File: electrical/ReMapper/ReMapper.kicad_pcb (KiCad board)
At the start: 4 copper layers, 35 x 65 mm, 43 parts, among them J1 ESP_UART0, J2 I2C Display, J3 USB_IN, J4 USB_OUT, J5 Button GND Pad, J9 Button Socket, U1 SPX1117M3-L-3-3/TR, U2 W25Q128JVE, U3 ESP32-S3-WROOM-1-N8R8, U4 RP2040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

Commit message: started working on v5
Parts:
- removed G***: LOGO, LOGO
- removed J1: ESP_UART0, Connector_PinHeader_1.27mm:PinHeader_1x04_P1.27mm_Vertical_SMD_Pin1Right
- removed J9: Button Socket, Connector_PinHeader_1.27mm:PinHeader_1x04_P1.27mm_Vertical_SMD_Pin1Left
- removed JP1: RP2040 Prog, Jumper:SolderJumper-2_P1.3mm_Open_RoundedPad1.0x1.5mm
- added S3: ESP_B1, generated_lscs:SW-SMD_4P-L4.5-W4.5-P3.00-LS6.8, F.Cu at (169.1, 115.0)
- added S4: ESP_B2, generated_lscs:SW-SMD_4P-L4.5-W4.5-P3.00-LS6.8, F.Cu at (185.1, 115.0)
- added S5: ESP_B3, generated_lscs:SW-SMD_4P-L4.5-W4.5-P3.00-LS6.8, F.Cu at (200.8, 115.0)
- added S6: ESP_B4_prog, generated_lscs:SW-SMD_4P-L4.5-W4.5-P3.00-LS6.8, F.Cu at (150.8, 115.0)
- C10, C13, C14, U4, U5: moved to B.Cu
- J2: footprint Connector_PinHeader_1.27mm:PinHeader_1x04_P1.27mm_Vertical -> Connector_PinHeader_2.54mm:PinHeader_1x04_P2.54mm_Vertical; moved to F.Cu
- J5: value Button GND Pad -> Conn_01x06_Pin; footprint TestPoint:TestPoint_Pad_D2.0mm -> cedarhacks:pogo_pin_2.54mm
- moved J3 69.7 mm to (142.6, 90.2), turned to -90 degrees
- moved LED5 69.3 mm to (144.0, 106.0), turned to 0 degrees
- moved R8 66.8 mm to (147.6, 106.0), turned to 180 degrees
- moved LED3 65.6 mm to (144.0, 102.6), turned to 0 degrees
- moved R6 63.9 mm to (147.6, 102.6), turned to 180 degrees
- moved R1 56.9 mm to (148.0, 115.4), turned to 180 degrees
- moved S1 55.7 mm to (156.8, 116.4)
- moved C2 55.5 mm to (151.6, 115.4), turned to 180 degrees
- moved C11 54.8 mm to (204.7, 108.6), turned to 90 degrees
- moved Y1 52.4 mm to (200.7, 108.4), turned to 180 degrees
- moved D1 51.9 mm to (154.1, 105.5), turned to 180 degrees
- moved C12 51.5 mm to (197.0, 109.4), turned to -90 degrees
- moved C8 51.4 mm to (165.1, 117.8), turned to -90 degrees
- moved D2 51.0 mm to (154.2, 103.9), turned to 0 degrees
- moved R2 50.4 mm to (196.2, 106.4), turned to 180 degrees
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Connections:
- J5 pad 1: GND -> /3.3V
- R5 pad 1: Net-(JP1-B) -> /RP2040_PROG
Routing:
- net GND: track 71.6 -> 0.00 mm, vias 26 -> 0
- net /USB_VIN: track 68.6 -> 0.00 mm, vias 3 -> 0
- net /USB_OUT_D-: track 45.8 -> 0.00 mm, vias 2 -> 0
- net /USB_OUT_D+: track 45.8 -> 0.00 mm, vias 1 -> 0
- net /3.3V: track 40.1 -> 0.00 mm, vias 17 -> 0
- net /QSPI_IO0_esp: track 38.3 -> 0.00 mm, vias 2 -> 0
- net /SPI2_MISO: track 37.8 -> 0.00 mm, vias 1 -> 0
- net /QSPI_CLK_esp: track 36.7 -> 0.00 mm, vias 2 -> 0
- net /SPI2_CLK: track 36.4 -> 0.00 mm, vias 1 -> 0
- net /QSPI_IO3_esp: track 35.4 -> 0.00 mm
- net /QSPI_IO2_esp: track 33.8 -> 0.00 mm, vias 2 -> 0
- net /SPI2_CS: track 32.2 -> 0.00 mm, vias 1 -> 0
- net /SPI2_MOSI: track 31.7 -> 0.00 mm, vias 1 -> 0
- net /QSPI_IO1_esp: track 31.1 -> 0.00 mm, vias 2 -> 0
- net /ESP_BUTTON_3: track 24.2 -> 0.00 mm, vias 1 -> 0
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- removed copper zone on In2.Cu, net /3.3V
- removed copper zone on In1.Cu, net GND
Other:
- board size 35 x 65 mm -> 75 x 55 mm
- board text removed: "3.3V"
- board text removed: "33V"
- board text removed: "33V LED"
- board text removed: "B1"
- board text removed: "B2"
- board text removed: "B3"
- board text removed: "CLK"
- board text removed: "D+"
- board text removed: "D-"
- board text removed: "DATA"
- board text removed: "ESP ENB"
- board text removed: "ESP LED"
- board text removed: "ESP UART"
- board text removed: "ESP prog"
- board text removed: "GND"
- board text removed: "PROG"
- board text removed: "RX"
- board text removed: "ReMapper Rev4 CedarHacks.com"
- board text removed: "TX"
- board text removed: "VIN"

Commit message: perhaps good layout
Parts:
- added ?: , , F.Cu at (189.8, 102.7)
- added ?: , , F.Cu at (189.8, 79.2)
- added ?: , , F.Cu at (166.8, 79.2)
- added ?: , , F.Cu at (166.8, 102.7)
- moved C13 4.56 mm to (189.1, 84.1)
- moved D3 4.04 mm to (160.4, 103.6)
- moved D4 4.04 mm to (160.4, 101.8)
- moved C14 3.06 mm to (189.1, 85.9)
- moved J3 0.19 mm to (142.6, 90.1)
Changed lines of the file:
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@@
 		)
 	)
+	(footprint ""
+		(layer "F.Cu")
+		(at 189.8176 102.681599)
+		(property "Reference" ""
+			(at 0 0 0)
+			(layer "F.SilkS")
+			(effects
+				(font
+					(size 1.27 1.27)
+					(thickness 0.15)
+				)
+			)
+		)
+		(property "Value" ""
+			(at 0 0 0)
+			(layer "F.Fab")
+			(effects
+				(font
+					(size 1.27 1.27)
+					(thickness 0.15)
+				)
+			)
+		)
+		(property "Datasheet" ""
+			(at 0 0 0)
+			(layer "F.Fab")
+			(hide yes)
+			(effects
+				(font
+					(size 1.27 1.27)
+					(thickness 0.15)
+				)
+			)
+		)
+		(property "Description" ""
+			(at 0 0 0)
+			(layer "F.Fab")
+			(hide yes)
+			(effects
+				(font
+					(size 1.27 1.27)
+					(thickness 0.15)
+				)
+			)
+		)
+		(pad "" np_thru_hole circle
+			(at 0 0)
+			(size 2.2 2.2)
+			(drill 2.2)
+			(layers "*.Cu" "*.Mask")
+		)
+		(embedded_fonts no)
+	)
 	(footprint "Resistor_SMD:R_0603_1608Metric"
 		(layer "F.Cu")
@@
 		)
 	)
+	(footprint ""
+		(layer "F.Cu")
+		(at 189.8176 79.181599)
+		(property "Reference" ""
+			(at 0 0 0)
+			(layer "F.SilkS")
+			(effects
+				(font
+					(size 1.27 1.27)
+					(thickness 0.15)
+				)
+			)
+		)
+		(property "Value" ""
+			(at 0 0 0)
+			(layer "F.Fab")
+			(effects
+				(font
+					(size 1.27 1.27)
+					(thickness 0.15)
+				)
+			)
+		)
+		(property "Datasheet" ""
+			(at 0 0 0)
+			(layer "F.Fab")
+			(hide yes)
+			(effects
+				(font
+					(size 1.27 1.27)
+					(thickness 0.15)
+				)
+			)
+		)
+		(property "Description" ""
+			(at 0 0 0)
+			(layer "F.Fab")
+			(hide yes)
+			(effects
+				(font
+					(size 1.27 1.27)
+					(thickness 0.15)
+				)
+			)
+		)
+		(pad "" np_thru_hole circle
+			(at 0 0)
+			(size 2.2 2.2)
+			(drill 2.2)
+			(layers "*.Cu" "*.Mask")
+		)
+		(embedded_fonts no)
+	)
 	(footprint "generated_lscs:SW-SMD_4P-L4.5-W4.5-P3.00-LS6.8"
 		(layer "F.Cu")
@@
 			(at -3.068401 3.2424 180)
 			(layer "F.Fab")
+			(hide yes)
 			(effects
 				(font
@@
 			(at 0 1.43 90)
 			(layer "F.Fab")
+			(hide yes)
 			(effects
 				(font
@@
 	(footprint "footprints:USBA_Female"
 		(layer "F.Cu")
-		(at 142.565 90.25 -90)
+		(at 142.565 90.059 -90)
 		(property "Reference" "J3"
 			(at 9.191 -6.025 90)
@@
 		(embedded_fonts no)
 	)
+	(footprint ""
+		(layer "F.Cu")
+		(at 166.8176 79.181599)
+		(property "Reference" ""
+			(at 0 0 0)
+			(layer "F.SilkS")
+			(effects
+				(font
+					(size 1.27 1.27)
+					(thickness 0.15)
+				)
+			)
+		)
+		(property "Value" ""
+			(at 0 0 0)
+			(layer "F.Fab")
+			(effects
+				(font
+					(size 1.27 1.27)
+					(thickness 0.15)
+				)
+			)
+		)
+		(property "Datasheet" ""
+			(at 0 0 0)
+			(layer "F.Fab")
+			(hide yes)
+			(effects
+				(font
+					(size 1.27 1.27)
+					(thickness 0.15)
+				)
+			)
+		)
+		(property "Description" ""
+			(at 0 0 0)
+			(layer "F.Fab")
+			(hide yes)
+			(effects
+				(font
+					(size 1.27 1.27)
+					(thickness 0.15)
+				)
+			)
+		)
+		(pad "" np_thru_hole circle
+			(at 0 0)
+			(size 2.2 2.2)
+			(drill 2.2)
+			(layers "*.Cu" "*.Mask")
+		)
+		(embedded_fonts no)
+	)
 	(footprint "Capacitor_SMD:C_0603_1608Metric"
 		(layer "F.Cu")
@@
 		)
 	)
+	(footprint ""
+		(layer "F.Cu")
+		(at 166.8176 102.681599)
+		(property "Reference" ""
+			(at 0 0 0)
+			(layer "F.SilkS")
+			(effects
+				(font
+					(size 1.27 1.27)
+					(thickness 0.15)
+				)
+			)
+		)
+		(property "Value" ""
+			(at 0 0 0)
+			(layer "F.Fab")
+			(effects
+				(font
+					(size 1.27 1.27)
+					(thickness 0.15)
+				)
+			)
+		)
+		(property "Datasheet" ""
+			(at 0 0 0)
+			(layer "F.Fab")
+			(hide yes)
+			(effects
+				(font
+					(size 1.27 1.27)
+					(thickness 0.15)
+				)
+			)
+		)
+		(property "Description" ""
+			(at 0 0 0)
+			(layer "F.Fab")
+			(hide yes)
+			(effects
+				(font
+					(size 1.27 1.27)
+					(thickness 0.15)
+				)
+			)
+		)
+		(pad "" np_thru_hole circle
+			(at 0 0)
+			(size 2.2 2.2)
+			(drill 2.2)
+			(layers "*.Cu" "*.Mask")
+		)
+		(embedded_fonts no)
+	)
 	(footprint "Capacitor_SMD:C_0603_1608Metric"
 		(layer "F.Cu")
@@
 	(footprint "Capacitor_SMD:C_0603_1608Metric"
 		(layer "B.Cu")
-		(at 190.005 82.931 180)
+		(at 189.0906 85.852 180)
 		(descr "Capacitor SMD 0603 (1608 Metric), square (rectangular) end terminal, IPC-7351 nominal, (Body size source: IPC-SM-782 page 76, https://www.pcb-3d.com/wordpress/wp-content/uploads/ipc-sm-782a_amendment_1_and_2.pdf), generated with kicad-footprint-generator")
 		(tags "capacitor")
 		(property "Reference" "C14"
-			(at 0 1.43 0)
+			(at 3.0102 -0.0762 0)
 			(layer "B.SilkS")
 			(effects
@@
 		(tags "2.4 GHz Wi-Fi and Bluetooth module")
 		(property "Reference" "U3"
-			(at -10.5 -11.4 90)
+			(at -8.4694 -14.1516 0)
 			(unlocked yes)
 			(layer "B.SilkS")
@@
 	(footprint "Diode_SMD:D_SOD-523"
 		(layer "B.Cu")
-		(at 164.403 103.505)
+		(at 160.3644 103.6066)
 		(descr "http://www.diodes.com/datasheets/ap02001.pdf p.144")
 		(tags "Diode SOD523")
@@
 	(footprint "Capacitor_SMD:C_0603_1608Metric"
 		(layer "B.Cu")
-		(at 190.018 79.659 180)
+		(at 189.103 84.1248 180)
 		(descr "Capacitor SMD 0603 (1608 Metric), square (rectangular) end terminal, IPC-7351 nominal, (Body size source: IPC-SM-782 page 76, https://www.pcb-3d.com/wordpress/wp-content/uploads/ipc-sm-782a_amendment_1_and_2.pdf), generated with kicad-footprint-generator")
 		(tags "capacitor")
 		(property "Reference" "C13"
-			(at 0 1.43 0)
+			(at 3.048 -0.0762 0)
 			(layer "B.SilkS")
 			(effects
@@
 	(footprint "Diode_SMD:D_SOD-523"
 		(layer "B.Cu")
-		(at 164.403 101.727)
+		(at 160.3644 101.8286)
 		(descr "http://www.diodes.com/datasheets/ap02001.pdf p.144")
 		(tags "Diode SOD523")

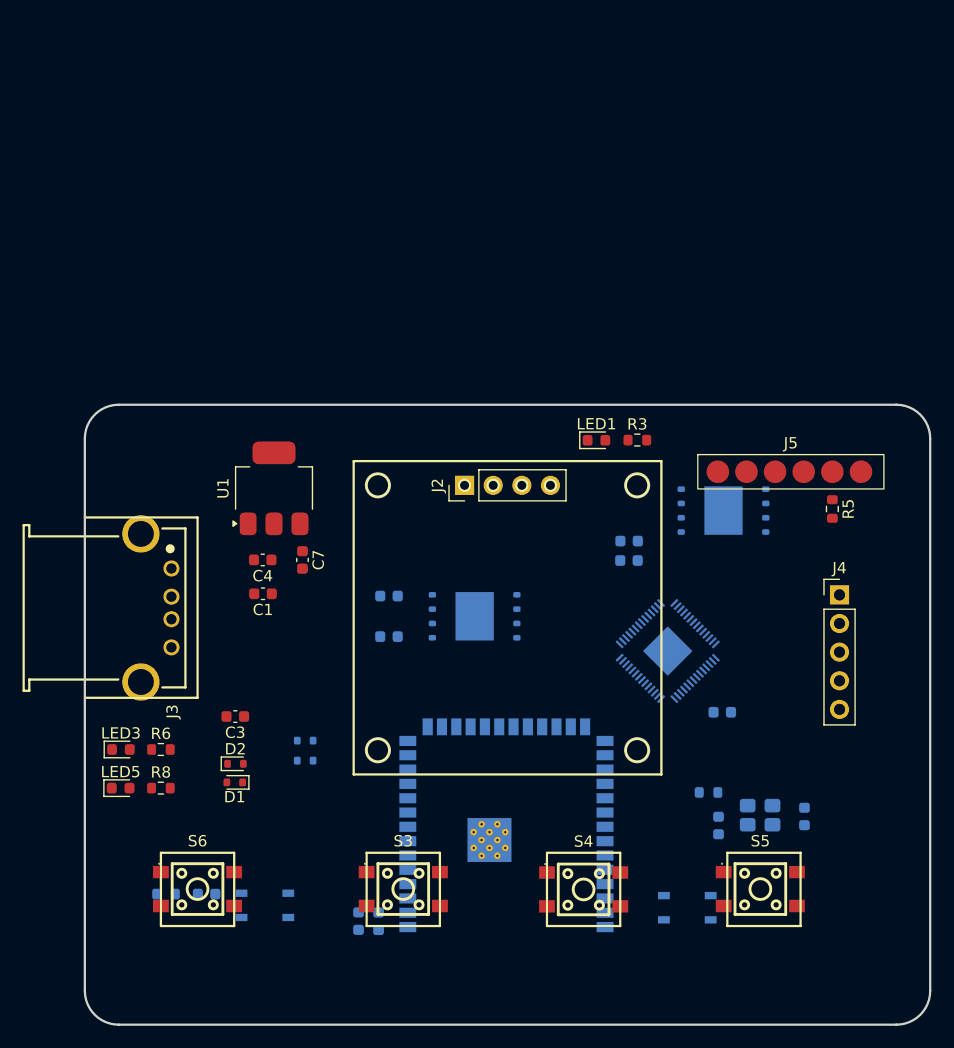
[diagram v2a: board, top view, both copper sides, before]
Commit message: dip switch, more layout fixes
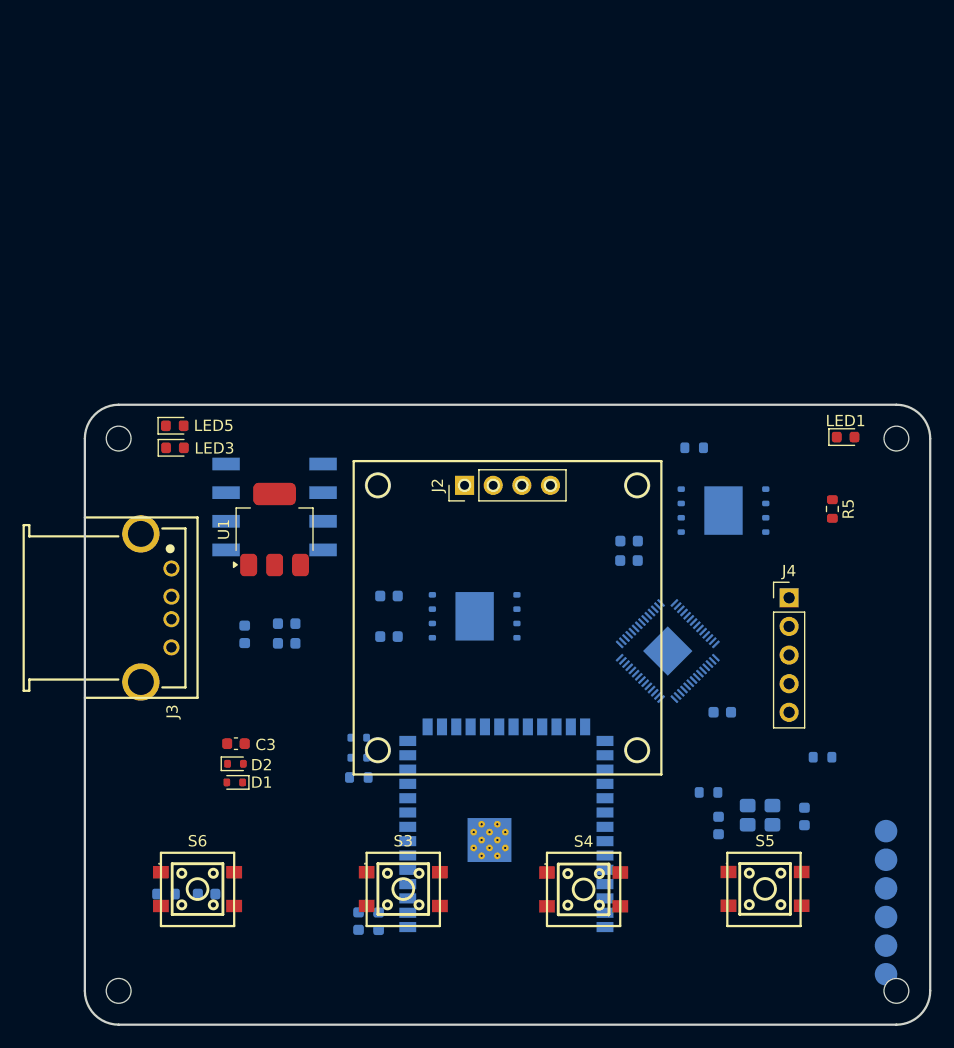
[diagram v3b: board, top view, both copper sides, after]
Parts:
- removed S1, S2: SKRPABE010, footprints:push_button_SKRPABE010
- added ?: , , F.Cu at (212.8, 124.0)
- added ?: , , F.Cu at (143.8, 124.0)
- added ?: , , F.Cu at (212.8, 75.0)
- added ?: , , F.Cu at (143.8, 75.0)
- added SW1: Programming Pins, footprints:SW_DIP_219-4, B.Cu at (157.7, 81.1)
- C1, C4, C7, R3, R6, R8: moved to B.Cu
- J5: value Conn_01x06_Pin -> PogoPIN; moved to B.Cu
- moved R6 58.7 mm to (206.3, 103.3)
- moved J5 39.2 mm to (211.9, 116.2), turned to 90 degrees
- moved LED5 32.5 mm to (148.8, 73.9)
- moved LED3 27.2 mm to (148.8, 75.8)
- moved LED1 22.1 mm to (208.3, 74.9)
- moved R8 17.6 mm to (165.1, 105.1)
- moved C7 8.36 mm to (155.0, 92.4)
- moved C4 6.04 mm to (158.7, 91.5), turned to 0 degrees
- moved R3 5.09 mm to (194.9, 75.8), turned to 0 degrees
- moved C1 4.88 mm to (158.7, 93.2), turned to 0 degrees
- moved D3 4.76 mm to (165.1, 103.3)
- moved D4 4.76 mm to (165.1, 101.6)
- moved J4 4.48 mm to (203.3, 89.2)
- moved U1 3.65 mm to (157.7, 83.1)
- moved C3 2.41 mm to (154.2, 102.1)
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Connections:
- net Net-(U3-EN) renamed /ESP_EN
- J5 pad 5: /RP2040_PROG -> unconnected-(J5-Pin_5-Pad5)

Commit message: passing DRC
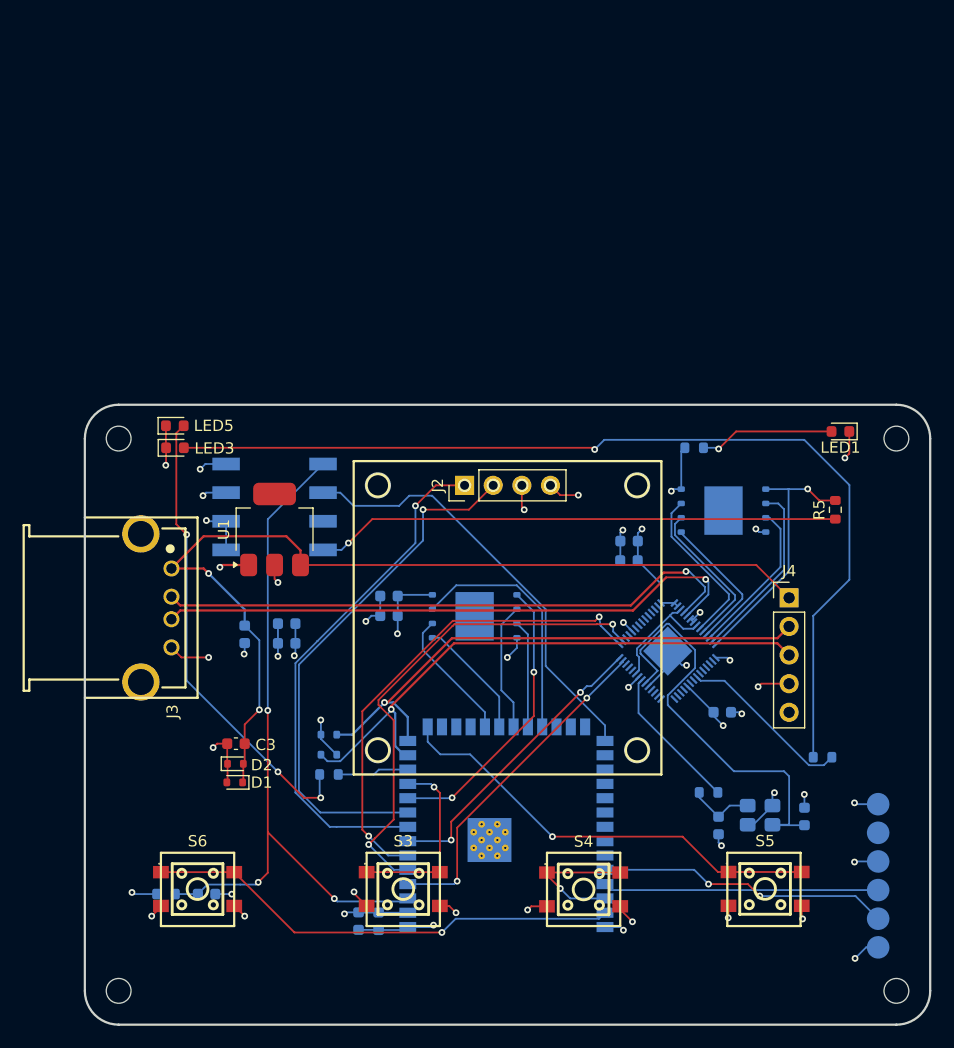
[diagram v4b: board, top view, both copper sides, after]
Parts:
- moved D3 2.66 mm to (162.5, 103.1)
- moved D4 2.66 mm to (162.5, 101.3)
- moved R8 2.66 mm to (162.5, 104.8)
- moved J5 2.49 mm to (211.2, 113.8)
- moved C6 1.85 mm to (167.8, 90.8)
- moved LED1 0.68 mm to (207.8, 74.4), turned to 180 degrees
- moved R5 0.27 mm to (207.4, 81.3), turned to 90 degrees
- turned C2 to 0 degrees
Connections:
- S6 pad 1: Net-(S6-Pad1) -> /PROG_MODE_ENB
- S6 pad 2: Net-(S6-Pad1) -> /PROG_MODE_ENB
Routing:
- net GND: track 0.00 -> 88.2 mm, vias 0 -> 35
- net Net-(LED3-A): track 0.00 -> 86.6 mm, vias 0 -> 1
- net /USB_VIN: track 0.00 -> 83.5 mm, vias 0 -> 2
- net /ESP_EN: track 0.00 -> 62.4 mm, vias 0 -> 3
- net /USB_IN_D+: track 0.00 -> 53.1 mm, vias 0 -> 1
- net /USB_IN_D-: track 0.00 -> 52.5 mm, vias 0 -> 1
- net /USB_OUT_D+: track 0.00 -> 51.6 mm, vias 0 -> 1
- net /USB_OUT_D-: track 0.00 -> 48.8 mm, vias 0 -> 1
- net /3.3V: track 0.00 -> 47.8 mm, vias 0 -> 14
- net /I2C_CLK_DISPLAY: track 0.00 -> 47.1 mm, vias 0 -> 1
- net /RP2040_PROG: track 0.00 -> 46.6 mm, vias 0 -> 1
- net /I2C_DATA_DISPLAY: track 0.00 -> 46.2 mm, vias 0 -> 1
- net /SPI2_MISO: track 0.00 -> 44.1 mm, vias 0 -> 2
- net /SPI2_CLK: track 0.00 -> 43.1 mm, vias 0 -> 2
- net /PROG_MODE_ENB: track 0.00 -> 42.3 mm, vias 0 -> 1
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- added copper zone on In2.Cu, net /3.3V
- added copper zone on In1.Cu, net GND
